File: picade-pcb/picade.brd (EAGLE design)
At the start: 80 x 50 mm, 60 parts, among them P1JOY 2.54MM-5P-SCREW-TERMINALLOCK, P2JOY 2.54MM-5P-SCREW-TERMINALLOCK

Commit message: Production candidate
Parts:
- removed COIN, P1JOY, P2JOY, UTILITY: 2.54MM-5P-SCREW-TERMINALLOCK, pimoroni:2.54MM-5P-SCREW-TERMINAL
- removed JP4, JP5: (no value), SparkFun-Connectors:1X05_LOCK
- removed R4: 47KR, resistor:R0603
- added BUTTONS1: 2.54MM-7P-SCREW-TERMINALLOCK, pimoroni:2.54MM-7P-SCREW-TERMINAL
- added C16: 100nF, resistor:C0805K
- added JOYSTICK: 2.54MM-5P-SCREW-TERMINALLOCK, pimoroni:2.54MM-5P-SCREW-TERMINAL
- 16MHZ: value (none) -> TSX-3225; device adafruit:NX5032 -> pimoroni:TSX-3225
- C3: value 100uF -> 100nF; device resistor:153CLV-0605 -> resistor:C0603K
- JP3: device SparkFun-Connectors:1X05_LOCK -> SparkFun-Connectors:1X07_LOCK
- moved R3 38.8 mm to (49.5, 1.52), turned to 0 degrees
- moved JP3 32.0 mm to (6.16, 37.8)
- moved R2 31.6 mm to (49.6, 14.8), turned to 0 degrees
- moved RESET 22.4 mm to (44.5, 34.0)
- moved RN1 19.6 mm to (36.8, 34.9)
- moved C3 18.4 mm to (38.0, 24.5)
- moved R7 15.7 mm to (39.0, 30.2)
- moved C13 12.7 mm to (44.6, 3.71), turned to 0 degrees
- moved BUTTONS 11.0 mm to (31.6, 3.22)
- moved JP1 11.0 mm to (22.7, 8.19)
- moved C12 10.7 mm to (30.7, 34.4)
- moved F1 10.1 mm to (56.4, 32.3)
- moved 16MHZ 9.77 mm to (27.6, 34.5)
- moved C8 9.62 mm to (32.2, 15.3)
- moved C10 9.38 mm to (34.9, 16.3), turned to 270 degrees
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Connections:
- net IN5 renamed BUTTON5
- net IN6 renamed BUTTON6
- net LINEINL renamed LINEINL+
- net LINEINR renamed LINEINR+
- net N$15 renamed VBUS
- removed net BCOM: ATMEGA32U4.30, BUTTONS.1, JP1.1
- removed net CSCOM: ATMEGA32U4.26, COIN.1, JP4.1
- removed net IN1: ATMEGA32U4.36, BUTTONS.2, COIN.5, JP1.2, JP2.2, JP3.5, JP4.5, JP5.3, P1JOY.2, P2JOY.5, UTILITY.3
- removed net IN2: ATMEGA32U4.37, BUTTONS.3, COIN.4, JP1.3, JP2.3, JP3.4, JP4.4, JP5.4, P1JOY.3, P2JOY.4, UTILITY.4
- removed net IN3: ATMEGA32U4.38, BUTTONS.4, COIN.3, JP1.4, JP2.4, JP3.3, JP4.3, JP5.5, P1JOY.4, P2JOY.3, UTILITY.5
- removed net IN4: ATMEGA32U4.39, BUTTONS.5, COIN.2, JP1.5, JP2.5, JP3.2, JP4.2, P1JOY.5, P2JOY.2
- removed net MODESHIFT: ATMEGA32U4.25, JP5.2, R4.1, UTILITY.2
- removed net P1JCOM: ATMEGA32U4.28, JP2.1, P1JOY.1
- removed net P2JCOM: ATMEGA32U4.29, JP3.1, P2JOY.1
- removed net SHDWN: U$4.3
- removed net UCOM: ATMEGA32U4.27, JP5.1, UTILITY.1
- new net BUTTON1: ATMEGA32U4.36, BUTTONS.2, JP1.2
- new net BUTTON2: ATMEGA32U4.37, BUTTONS.3, JP1.3
- new net BUTTON3: ATMEGA32U4.38, BUTTONS.4, JP1.4
- new net BUTTON4: ATMEGA32U4.39, BUTTONS.5, JP1.5
- new net COIN: ATMEGA32U4.25, BUTTONS1.3, JP3.3
- new net DOWN: ATMEGA32U4.28, JOYSTICK.3, JP2.3
- new net ENTER: ATMEGA32U4.20, BUTTONS1.5, JP3.5
- new net ESCAPE: ATMEGA32U4.21, BUTTONS1.4, JP3.4
- new net LEFT: ATMEGA32U4.29, JOYSTICK.4, JP2.4
- new net LINEIN-: C14.1, HEADPHONES.SLEEVE, LINEIN.SLEEVE
- new net RIGHT: ATMEGA32U4.30, JOYSTICK.5, JP2.5
- new net START: ATMEGA32U4.26, BUTTONS1.2, JP3.2
- new net UP: ATMEGA32U4.27, JOYSTICK.2, JP2.2
- new net VOLUMEDOWN: ATMEGA32U4.19, BUTTONS1.6, JP3.6
- new net VOLUMEUP: ATMEGA32U4.18, BUTTONS1.7, JP3.7
- net 5V: now also C16.1, C3.1, U$4.3; no longer C3.+, R4.2
- net GND: now also 16MHZ.2, 16MHZ.4, BUTTONS.1, BUTTONS1.1, C16.2, C3.2, JOYSTICK.1, JP1.1, JP2.1, JP3.1; no longer C14.1, C3.-, HEADPHONES.SLEEVE, LINEIN.SLEEVE
- net VDOWN: now also ATMEGA32U4.1; no longer ATMEGA32U4.19
- net VUP: now also ATMEGA32U4.12; no longer ATMEGA32U4.18
- net XTAL1: now also 16MHZ.1; no longer 16MHZ.P$2
- net XTAL2: now also 16MHZ.3; no longer 16MHZ.P$1
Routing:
- net IN3: track 125.7 -> 0.00 mm, vias 1 -> 0
- net IN2: track 118.0 -> 0.00 mm, vias 1 -> 0
- net IN1: track 114.1 -> 0.00 mm, vias 1 -> 0
- net IN4: track 99.7 -> 0.00 mm, vias 1 -> 0
- net LINEIN-: track 0.00 -> 89.3 mm, vias 0 -> 2
- net MODESHIFT: track 40.8 -> 0.00 mm, vias 1 -> 0
- net P1JCOM: track 40.6 -> 0.00 mm, vias 1 -> 0
- net UCOM: track 35.0 -> 0.00 mm
- net CSCOM: track 33.4 -> 0.00 mm
- net START: track 0.00 -> 31.3 mm
- net UP: track 0.00 -> 31.2 mm
- net DOWN: track 0.00 -> 28.7 mm
- net COIN: track 0.00 -> 28.3 mm
- net P2JCOM: track 26.3 -> 0.00 mm, vias 1 -> 0
- net LEFT: track 0.00 -> 25.6 mm
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- added copper zone on layer 1, net VBUS
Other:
- board size 80 x 50 mm -> 71 x 46 mm
- board text added: "5V MOSI GND"
- board text added: "MISO SCK RST"
- board text added: "RESET/ICSP"
- board text added: "START COIN ESCAPE ENTER"
- board text added: "v2.03"
- board text removed: "5V"
- board text removed: "GND"
- board text removed: "MISO"
- board text removed: "MOSI"
- board text removed: "P1"
- board text removed: "P2"
- board text removed: "RESET"
- board text removed: "RST"
- board text removed: "SCK"
- board text removed: "v2.00"
- board text removed: "v2.02"

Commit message: New layout - pending silkage!
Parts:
- removed BUTTONS, BUTTONS1: 2.54MM-7P-SCREW-TERMINALLOCK, pimoroni:2.54MM-7P-SCREW-TERMINAL
- removed JOYSTICK: 2.54MM-5P-SCREW-TERMINALLOCK, pimoroni:2.54MM-5P-SCREW-TERMINAL
- removed JP1, JP3: (no value), SparkFun-Connectors:1X07_LOCK
- removed JP2: (no value), SparkFun-Connectors:1X05_LOCK
- removed SPEAKERS: 2.54MM-4P-SCREW-TERMINALLOCK, pimoroni:2.54MM-4P-SCREW-TERMINAL
- added U$10, U$11, U$12, U$9: (no value), pimoroni-misc:M3-MOUNTING-HOLE
- added U$5: 5-WAY, pimoroni-headers:1X5-3.5MM-SCREWTERMINAL
- added U$6, U$7: 7-WAY, pimoroni-headers:1X7-3.5MM-SCREWTERMINAL
- added U$8: 4-WAY, pimoroni-headers:1X4-3.5MM-SCREWTERMINAL
- moved RX 15.1 mm to (67.0, 58.2)
- moved F1 15.0 mm to (65.4, 44.3)
- moved L5 15.0 mm to (71.0, 44.3)
- moved R5 15.0 mm to (66.1, 47.3)
- moved R6 15.0 mm to (69.6, 47.3)
- moved USB 15.0 mm to (78.6, 48.0)
- moved U$1 14.9 mm to (11.6, 51.4)
- moved TX 14.5 mm to (67.0, 55.5)
- moved BL 13.9 mm to (67.0, 52.8)
- moved RN1 13.8 mm to (45.8, 45.4)
- moved C9 13.5 mm to (47.0, 32.9)
- moved R7 13.5 mm to (48.0, 40.2)
- moved ATMEGA32U4 13.5 mm to (38.0, 33.2)
- moved C10 13.5 mm to (43.9, 26.3)
- moved C11 13.5 mm to (33.5, 44.5)
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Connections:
- net BUTTON1: now also U$6.7; no longer BUTTONS.2, JP1.2
- net BUTTON2: now also U$6.6; no longer BUTTONS.3, JP1.3
- net BUTTON3: now also U$6.5; no longer BUTTONS.4, JP1.4
- net BUTTON4: now also U$6.4; no longer BUTTONS.5, JP1.5
- net BUTTON5: now also U$6.3; no longer BUTTONS.6, JP1.6
- net BUTTON6: now also U$6.2; no longer BUTTONS.7, JP1.7
- net COIN: now also U$7.3; no longer BUTTONS1.3, JP3.3
- net DOWN: now also U$5.4; no longer JOYSTICK.3, JP2.3
- net ENTER: now also U$7.5; no longer BUTTONS1.5, JP3.5
- net ESCAPE: now also U$7.4; no longer BUTTONS1.4, JP3.4
- net GND: now also U$5.1, U$6.1, U$7.1; no longer BUTTONS.1, BUTTONS1.1, JOYSTICK.1, JP1.1, JP2.1, JP3.1
- net LEFT: now also U$5.3; no longer JOYSTICK.4, JP2.4
- net RIGHT: now also U$5.2; no longer JOYSTICK.5, JP2.5
- net SPEAKERL+: now also U$8.4; no longer SPEAKERS.4
- net SPEAKERL-: now also U$8.3; no longer SPEAKERS.3
- net SPEAKERR+: now also U$8.1; no longer SPEAKERS.1
- net SPEAKERR-: now also U$8.2; no longer SPEAKERS.2
- net START: now also U$7.2; no longer BUTTONS1.2, JP3.2
- net UP: now also U$5.5; no longer JOYSTICK.2, JP2.2
- net VOLUMEDOWN: now also U$7.6; no longer BUTTONS1.6, JP3.6
- net VOLUMEUP: now also U$7.7; no longer BUTTONS1.7, JP3.7
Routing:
- net VOLUMEUP: track 21.8 -> 44.7 mm
- net VOLUMEDOWN: track 21.2 -> 43.7 mm
- net ENTER: track 21.7 -> 40.8 mm
- net BUTTON1: track 15.8 -> 33.0 mm
- net BUTTON2: track 14.8 -> 30.1 mm
- net ESCAPE: track 23.6 -> 37.6 mm
- net LINEINL+: track 94.1 -> 80.9 mm
- net BUTTON3: track 14.9 -> 26.7 mm
- net COIN: track 28.3 -> 38.5 mm
- net BUTTON4: track 16.8 -> 26.1 mm
- net 5V: track 145.2 -> 154.0 mm
- net LINEINR+: track 82.5 -> 75.3 mm
- net RIGHT: track 24.4 -> 31.0 mm
- net BUTTON5: track 18.6 -> 24.6 mm
- net N$2: track 27.4 -> 21.7 mm
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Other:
- board size 71 x 46 mm -> 70 x 60 mm
- board text removed: "An Arduino compatible board designed for building arcade cabinets. UK's first Kickstarter!"
- board text removed: "Made in Sheffield, UK http://pimoroni.com"
- board text removed: "v2.03"

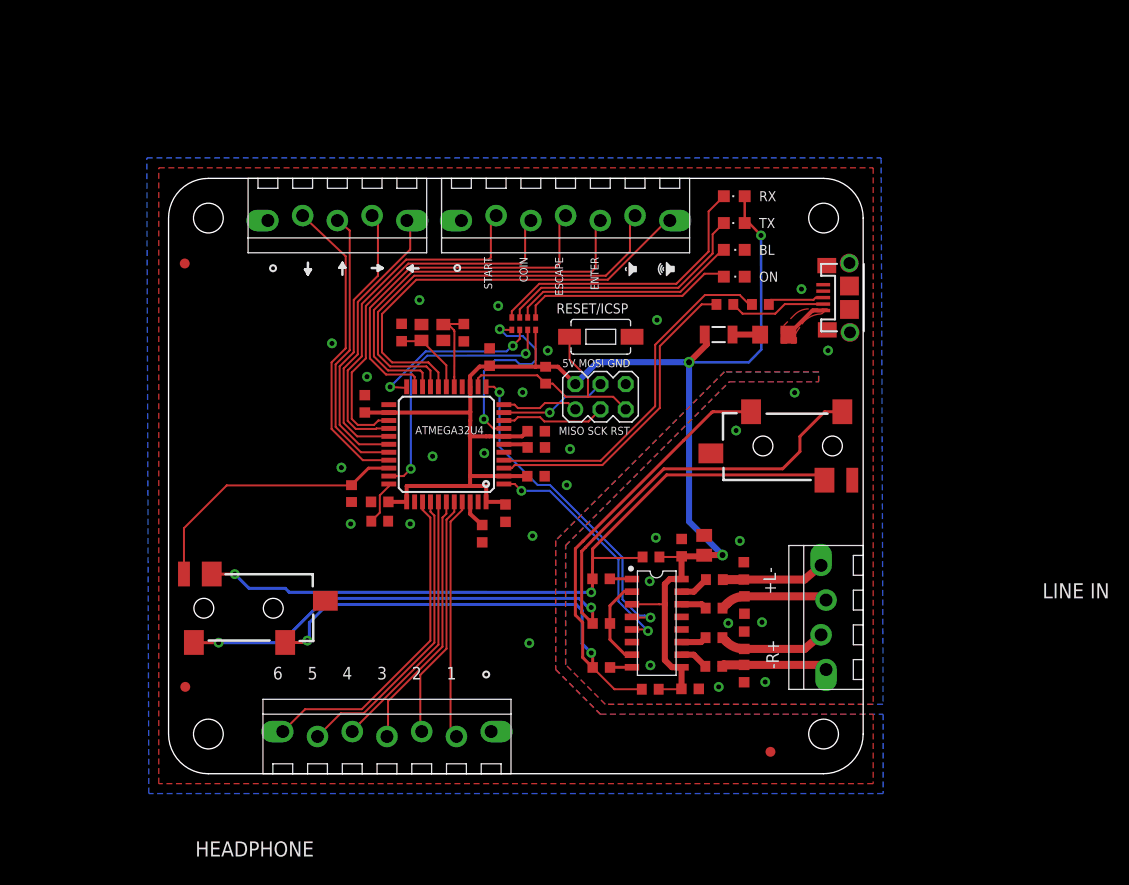
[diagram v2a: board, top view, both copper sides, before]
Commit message: Added USB shield decoupling
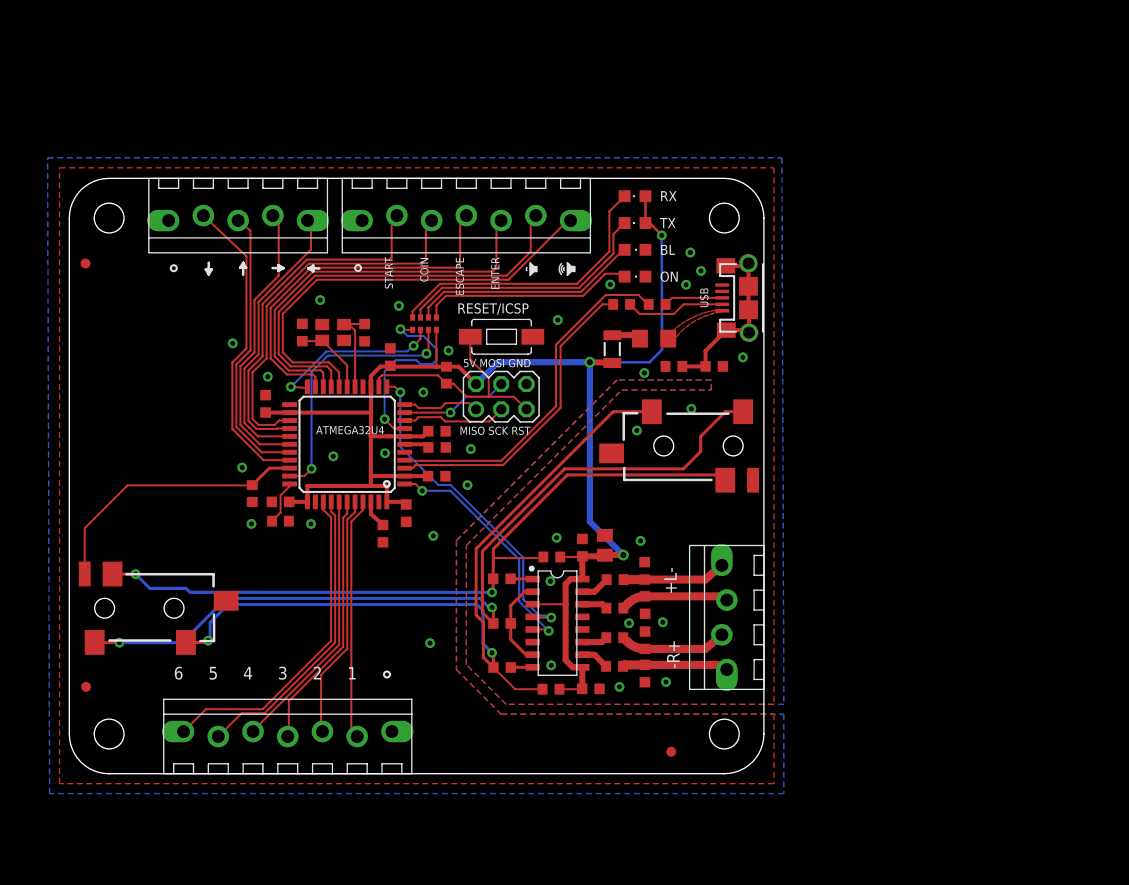
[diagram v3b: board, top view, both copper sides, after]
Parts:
- removed USB: USB-MICROB, pimoroni:USB-MICROB
- added C17: 4.7nF, resistor:C0603K
- added R4: 1M, resistor:R0603
- added U$13: USBMICROB, pimoroni-connectors:MICROB-USB
- moved L5 12.1 mm to (58.9, 43.8)
- moved F1 10.8 mm to (54.7, 42.8), turned to 270 degrees
- moved R5 10.4 mm to (55.6, 47.3)
- moved R6 10.4 mm to (59.2, 47.3)
- moved C23 10.0 mm to (58.0, 13.5)
- moved ATMEGA32U4 10.0 mm to (28.0, 33.2)
- moved BL 10.0 mm to (57.0, 52.8)
- moved C1 10.0 mm to (51.7, 22.8)
- moved C10 10.0 mm to (33.9, 26.3)
- moved C11 10.0 mm to (23.5, 44.5)
- moved C12 10.0 mm to (29.7, 44.4)
- moved C13 10.0 mm to (43.6, 10.7)
- moved C14 10.0 mm to (43.6, 15.1)
- moved C15 10.0 mm to (43.6, 19.6)
- moved C16 10.0 mm to (54.0, 23.0)
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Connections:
- new net SHIELD: C17.1, R4.2, U$13.SH1, U$13.SH2, U$13.SH3, U$13.SH4, U$13.SH5, U$13.SH6, U$13.SH7, U$13.SH8
- net GND: now also C17.2, R4.1, U$13.GND; no longer USB.GND, USB.MT1, USB.MT2, USB.P$1, USB.P$2, USB.P$3, USB.P$4
- net N$3: now also U$13.DM; no longer USB.D-
- net N$4: now also U$13.DP; no longer USB.D+
- net VBUS: now also U$13.VBUS; no longer USB.VBUS
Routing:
- net SHIELD: track 0.00 -> 18.6 mm
- net VBUS: track 4.52 -> 0.00 mm
- net 5V: track 154.0 -> 152.7 mm
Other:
- board text removed: "HEADPHONE"
- board text removed: "LINE IN"

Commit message: Minor tweaks
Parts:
- moved U$6 1.45 mm to (20.5, 4.04)
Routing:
- net BUTTON2: track 30.1 -> 31.5 mm
- net BUTTON1: track 33.0 -> 34.4 mm
- net BUTTON3: track 26.7 -> 28.1 mm
- net BUTTON4: track 26.1 -> 26.7 mm
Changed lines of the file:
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@@
 <element name="C3" library="resistor" package="C0603K" value="100nF" x="37.0362" y="34.5148" smashed="yes"/>
 <element name="U$5" library="pimoroni-headers" package="1X5-3.5MM-SCREWTERMINAL" value="5-WAY" x="17" y="56"/>
-<element name="U$6" library="pimoroni-headers" package="1X7-3.5MM-SCREWTERMINAL" value="7-WAY" x="22" y="4" rot="R180"/>
+<element name="U$6" library="pimoroni-headers" package="1X7-3.5MM-SCREWTERMINAL" value="7-WAY" x="20.5486" y="4.0386" rot="R180"/>
 <element name="U$7" library="pimoroni-headers" package="1X7-3.5MM-SCREWTERMINAL" value="7-WAY" x="40" y="56"/>
 <element name="U$8" library="pimoroni-headers" package="1X4-3.5MM-SCREWTERMINAL" value="4-WAY" x="66" y="15.75" rot="R270"/>
@@
 <element name="U$11" library="pimoroni-misc" package="M3-MOUNTING-HOLE" value="" x="66" y="4"/>
 <element name="U$12" library="pimoroni-misc" package="M3-MOUNTING-HOLE" value="" x="66" y="56"/>
-<element name="U$13" library="pimoroni-connectors" package="MICROB-USB" value="USBMICROB" x="68.4352" y="47.9552" rot="R90"/>
+<element name="U$13" library="pimoroni-connectors" package="MICROB-USB" value="USBMICROB" x="68.4352" y="47.9552" smashed="yes" rot="R90"/>
 <element name="C17" library="resistor" package="C0603K" value="4.7nF" x="64.9808" y="41.0464" smashed="yes"/>
 <element name="R4" library="resistor" package="R0603" value="1M" x="60.9168" y="41.0464" smashed="yes"/>
@@
 <contactref element="RN1" pad="6"/>
 <wire x1="23.983925" y1="38.998290625" x2="23.992434375" y2="38.8798" width="0.2032" layer="1"/>
-<wire x1="23.992434375" y1="38.8798" x2="22.3172" y2="38.9814" width="0.2032" layer="1"/>
-<via x="22.3172" y="38.9814" extent="1-16" drill="0.5"/>
-<wire x1="22.3172" y1="38.9814" x2="25.8986" y2="42.5628" width="0.2032" layer="16"/>
+<wire x1="23.992434375" y1="38.8798" x2="22.2156" y2="38.8798" width="0.2032" layer="1"/>
+<via x="22.2156" y="38.8798" extent="1-16" drill="0.5"/>
+<wire x1="22.2156" y1="38.8798" x2="25.8986" y2="42.5628" width="0.2032" layer="16"/>
 <wire x1="25.8986" y1="42.5628" x2="34.052" y2="42.5628" width="0.2032" layer="16"/>
 <wire x1="34.052" y1="42.5628" x2="34.6616" y2="43.1724" width="0.2032" layer="16"/>
@@
 <wire x1="29.583925" y1="26.579125" x2="28.4048" y2="25.4" width="0.2032" layer="1"/>
 <wire x1="28.4048" y1="25.4" x2="28.4048" y2="4.3452" width="0.2032" layer="1"/>
-<wire x1="28.4048" y1="4.3452" x2="29" y2="3.75" width="0.2032" layer="1"/>
+<wire x1="28.4048" y1="4.3452" x2="27.5486" y2="3.7886" width="0.2032" layer="1"/>
 </signal>
 <signal name="BUTTON5">
@@
 <wire x1="27.9984" y1="25.6032" x2="27.9984" y2="12.5984" width="0.2032" layer="1"/>
 <wire x1="27.9984" y1="12.5984" x2="25.3568" y2="9.9568" width="0.2032" layer="1"/>
-<wire x1="25.3568" y1="9.9568" x2="25.3568" y2="4.3932" width="0.2032" layer="1"/>
-<wire x1="25.3568" y1="4.3932" x2="25.5" y2="4.25" width="0.2032" layer="1"/>
+<wire x1="25.3568" y1="9.9568" x2="24.036" y2="8.6604" width="0.2032" layer="1"/>
+<wire x1="24.036" y1="8.6604" x2="24.0486" y2="4.2886" width="0.2032" layer="1"/>
 </signal>
 <signal name="RIGHT">
@@
 <wire x1="26.3728" y1="25.8064" x2="26.3728" y2="13.4112" width="0.2032" layer="1"/>
 <wire x1="26.3728" y1="13.4112" x2="19.464" y2="6.5024" width="0.2032" layer="1"/>
-<wire x1="19.464" y1="6.5024" x2="13.7524" y2="6.5024" width="0.2032" layer="1"/>
-<wire x1="13.7524" y1="6.5024" x2="11.5" y2="4.25" width="0.2032" layer="1"/>
+<wire x1="19.464" y1="6.5024" x2="12.2604" y2="6.5024" width="0.2032" layer="1"/>
+<wire x1="12.2604" y1="6.5024" x2="10.0486" y2="4.2886" width="0.2032" layer="1"/>
 </signal>
 <signal name="BUTTON2">
@@
 <wire x1="26.7792" y1="26.0096" x2="26.7792" y2="13.208" width="0.2032" layer="1"/>
 <wire x1="26.7792" y1="13.208" x2="19.6672" y2="6.096" width="0.2032" layer="1"/>
-<wire x1="19.6672" y1="6.096" x2="17.346" y2="6.096" width="0.2032" layer="1"/>
-<wire x1="17.346" y1="6.096" x2="15" y2="3.75" width="0.2032" layer="1"/>
+<wire x1="19.6672" y1="6.096" x2="15.8474" y2="6.096" width="0.2032" layer="1"/>
+<wire x1="15.8474" y1="6.096" x2="13.5486" y2="3.7886" width="0.2032" layer="1"/>
 </signal>
 <signal name="BUTTON3">
@@
 <contactref element="U$6" pad="5"/>
 <wire x1="27.183925" y1="27.398290625" x2="27.1856" y2="13.0048" width="0.2032" layer="1"/>
-<wire x1="27.1856" y1="13.0048" x2="18.5" y2="4.3192" width="0.2032" layer="1"/>
-<wire x1="18.5" y1="4.3192" x2="18.5" y2="4.25" width="0.2032" layer="1"/>
+<wire x1="27.1856" y1="13.0048" x2="18.4492" y2="4.2684" width="0.2032" layer="1"/>
+<wire x1="18.4492" y1="4.2684" x2="17.0486" y2="4.2886" width="0.2032" layer="1"/>
 </signal>
 <signal name="BUTTON4">
@@
 <wire x1="27.592" y1="25.8064" x2="27.592" y2="12.8016" width="0.2032" layer="1"/>
 <wire x1="27.592" y1="12.8016" x2="22.1056" y2="7.3152" width="0.2032" layer="1"/>
-<wire x1="22.1056" y1="7.3152" x2="22.1056" y2="3.8556" width="0.2032" layer="1"/>
-<wire x1="22.1056" y1="3.8556" x2="22" y2="3.75" width="0.2032" layer="1"/>
+<wire x1="22.1056" y1="7.3152" x2="20.5562" y2="5.7606" width="0.2032" layer="1"/>
+<wire x1="20.5562" y1="5.7606" x2="20.5486" y2="3.7886" width="0.2032" layer="1"/>
 </signal>
 <signal name="SHIELD">
